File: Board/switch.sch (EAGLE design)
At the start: 15 parts, among them IC2 LM1117

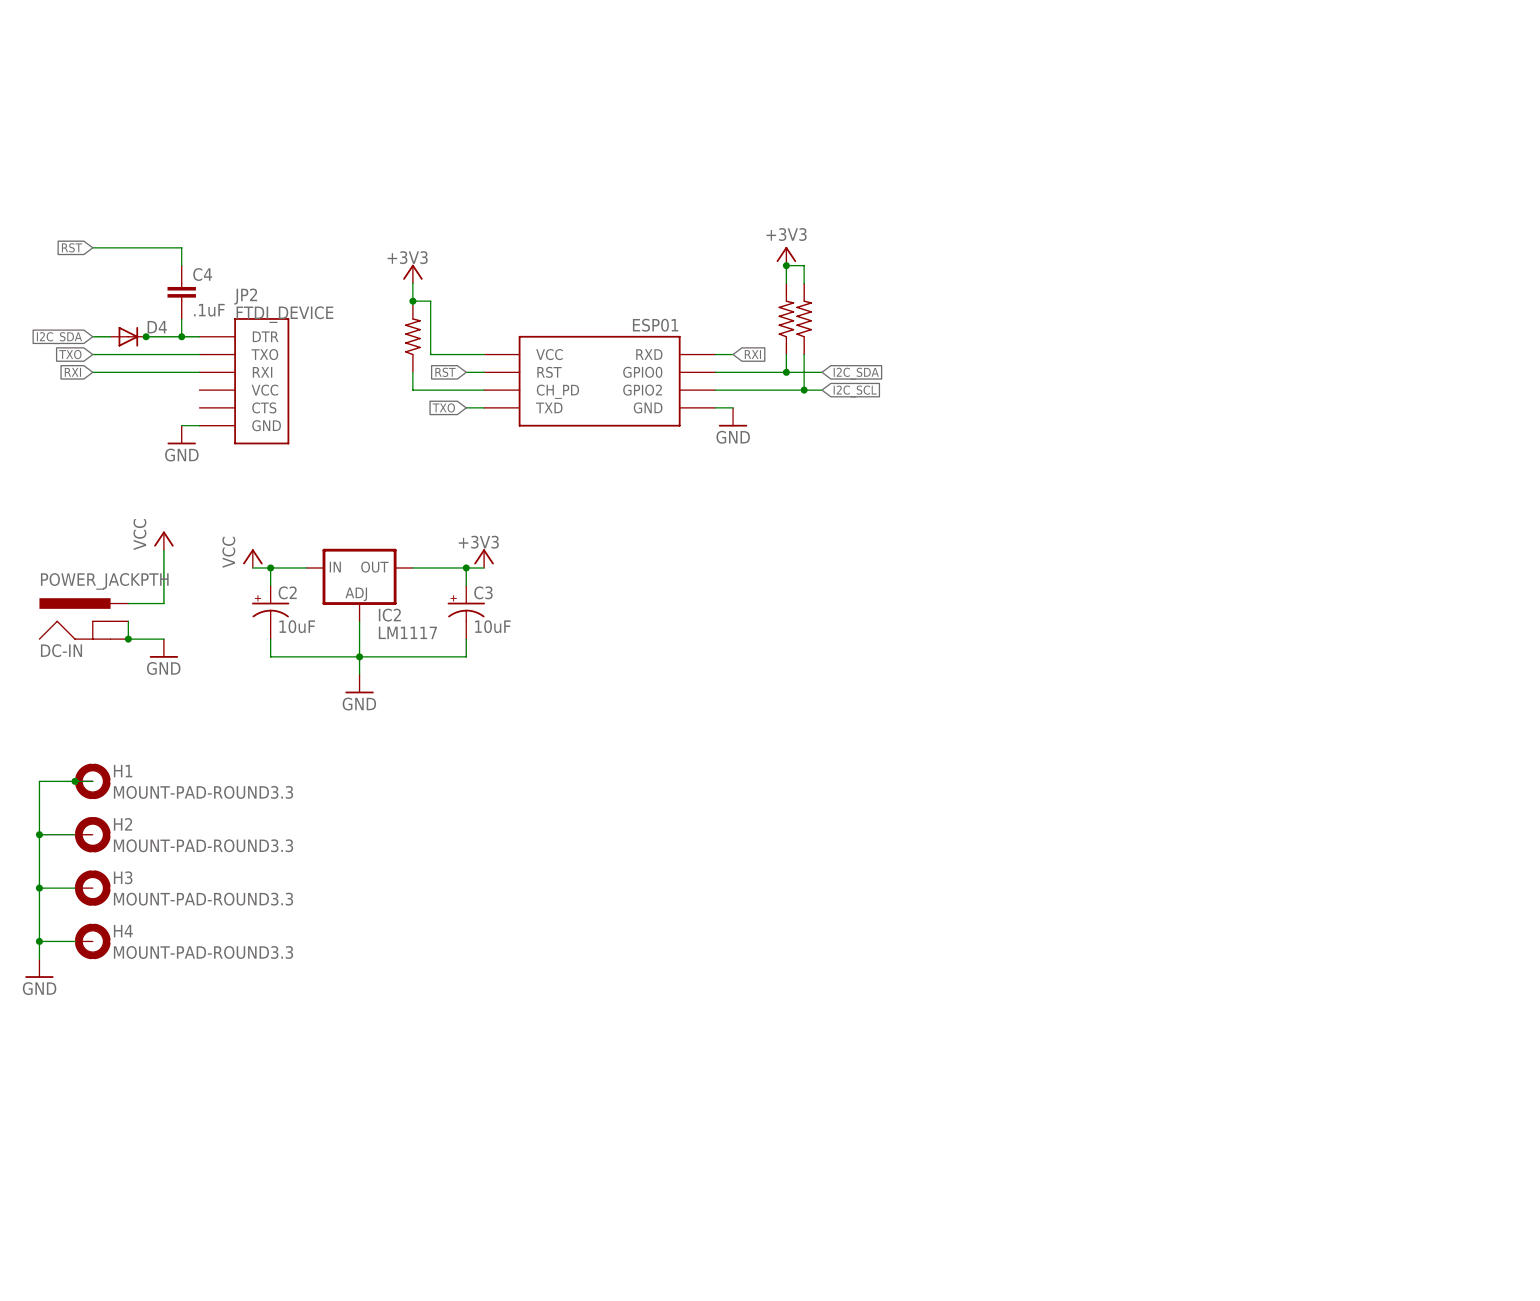
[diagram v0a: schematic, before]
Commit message: Add first pass board component layout
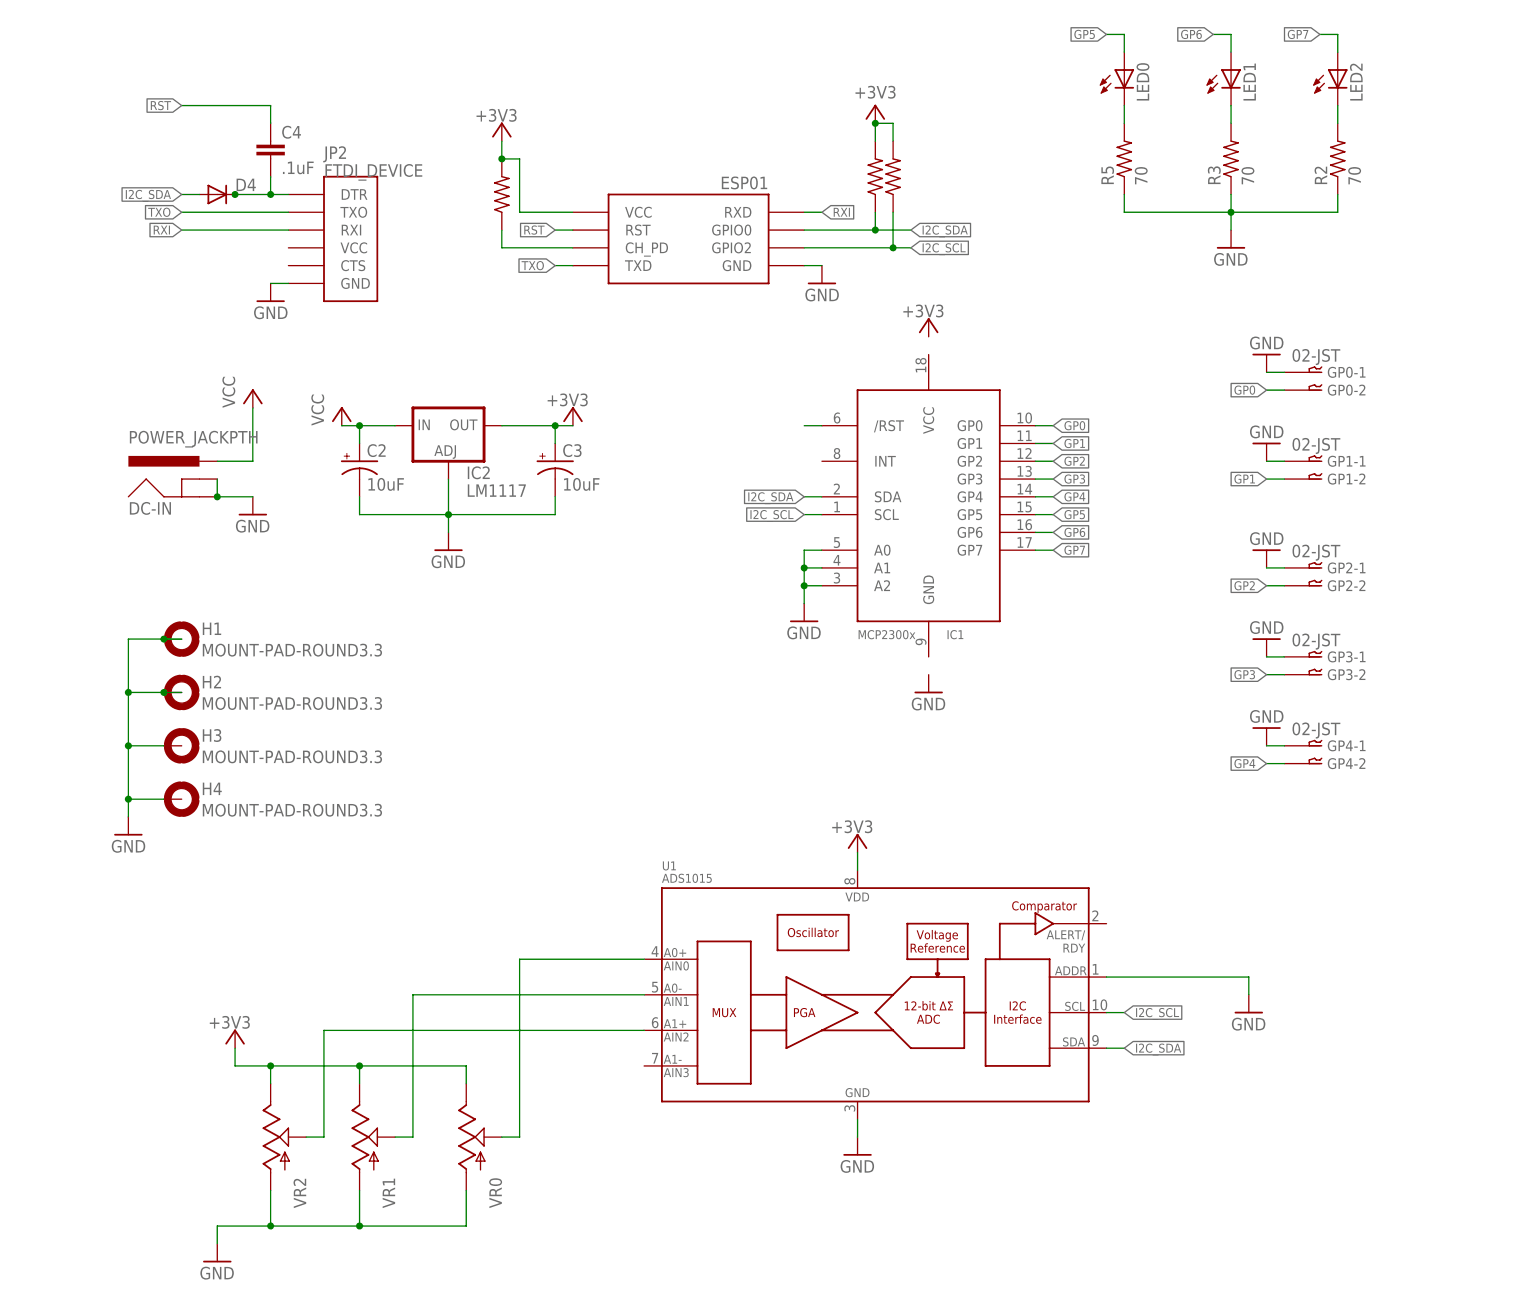
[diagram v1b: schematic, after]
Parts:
- added GP0, GP1, GP2, GP3, GP4: 02-JST, con-jst-xh:02-JST
- added IC1: MCP2300X/SO, adafruit:MCP2300X/SO
- added LED0, LED1, LED2: (no value), adafruit:LED3MM
- added R2, R3, R5: 70, resistor:R-US_R0603
- added U1: ADS1015, SparkFun-AnalogIC:ADS1015
- added VR0, VR1, VR2: (no value), SparkFun-Electromechanical:SLIDER30MM-KIT
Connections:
- new net DSD: GP2-1.1
- new net GP0: GP0-2.1, IC1.GP0
- new net GP1: GP1-2.1, IC1.GP1
- new net GP2: GP2-2.1, IC1.GP2
- new net GP3: GP3-2.1, IC1.GP3
- new net GP4: GP4-2.1, IC1.GP4
- new net GP5: IC1.GP5, LED0.A
- new net GP6: IC1.GP6, LED1.A
- new net GP7: IC1.GP7, LED2.A
- new net N$11: IC1./RST
- new net N$3: U1.AIN2, VR2.S
- new net N$4: U1.AIN1, VR1.S
- new net N$5: U1.AIN0, VR0.S
- new net N$6: LED0.C, R5.2
- new net N$7: LED1.C, R3.2
- new net N$8: LED2.C, R2.2
- net +3V3: now also U1.VDD, VR0.E, VR1.E, VR2.E
- net GND: now also GP0-1.1, GP1-1.1, GP3-1.1, GP4-1.1, IC1.A0, IC1.A1, IC1.A2, R2.1, R3.1, R5.1, U1.ADDR, U1.VSS, VR0.A, VR1.A, VR2.A
- net I2C_SCL: now also IC1.SCL, U1.SCL
- net I2C_SDA: now also IC1.SDA, U1.SDA
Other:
- moved on the sheet: C2, C3, C4, D4, DC-IN, H1, H2, H3, H4, IC2, JP2

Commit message: Use PTA3043 footprint for slider
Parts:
- VR0, VR1, VR2: device SparkFun-Electromechanical:SLIDER30MM-KIT -> SparkFun-Electromechanical:SLIDERPTA3043
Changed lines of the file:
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@@
 <grid distance="0.1" unitdist="inch" unit="inch" style="lines" multiple="1" display="no" altdistance="0.01" altunitdist="inch" altunit="inch"/>
 <layers>
-<layer number="1" name="Top" color="4" fill="1" visible="no" active="no"/>
-<layer number="2" name="Route2" color="1" fill="3" visible="no" active="no"/>
-<layer number="3" name="Route3" color="4" fill="3" visible="no" active="no"/>
-<layer number="14" name="Route14" color="1" fill="6" visible="no" active="no"/>
-<layer number="15" name="Route15" color="4" fill="6" visible="no" active="no"/>
-<layer number="16" name="Bottom" color="1" fill="1" visible="no" active="no"/>
-<layer number="17" name="Pads" color="2" fill="1" visible="no" active="no"/>
-<layer number="18" name="Vias" color="2" fill="1" visible="no" active="no"/>
-<layer number="19" name="Unrouted" color="6" fill="1" visible="no" active="no"/>
-<layer number="20" name="Dimension" color="15" fill="1" visible="no" active="no"/>
-<layer number="21" name="tPlace" color="7" fill="1" visible="no" active="no"/>
-<layer number="22" name="bPlace" color="7" fill="1" visible="no" active="no"/>
-<layer number="23" name="tOrigins" color="15" fill="1" visible="no" active="no"/>
-<layer number="24" name="bOrigins" color="15" fill="1" visible="no" active="no"/>
-<layer number="25" name="tNames" color="7" fill="1" visible="no" active="no"/>
-<layer number="26" name="bNames" color="7" fill="1" visible="no" active="no"/>
-<layer number="27" name="tValues" color="7" fill="1" visible="no" active="no"/>
-<layer number="28" name="bValues" color="7" fill="1" visible="no" active="no"/>
+<layer number="1" name="Top" color="4" fill="1" visible="yes" active="no"/>
+<layer number="2" name="Route2" color="1" fill="3" visible="yes" active="no"/>
+<layer number="3" name="Route3" color="4" fill="3" visible="yes" active="no"/>
+<layer number="14" name="Route14" color="1" fill="6" visible="yes" active="no"/>
+<layer number="15" name="Route15" color="4" fill="6" visible="yes" active="no"/>
+<layer number="16" name="Bottom" color="1" fill="1" visible="yes" active="no"/>
+<layer number="17" name="Pads" color="2" fill="1" visible="yes" active="no"/>
+<layer number="18" name="Vias" color="2" fill="1" visible="yes" active="no"/>
+<layer number="19" name="Unrouted" color="6" fill="1" visible="yes" active="no"/>
+<layer number="20" name="Dimension" color="15" fill="1" visible="yes" active="no"/>
+<layer number="21" name="tPlace" color="7" fill="1" visible="yes" active="no"/>
+<layer number="22" name="bPlace" color="7" fill="1" visible="yes" active="no"/>
+<layer number="23" name="tOrigins" color="15" fill="1" visible="yes" active="no"/>
+<layer number="24" name="bOrigins" color="15" fill="1" visible="yes" active="no"/>
+<layer number="25" name="tNames" color="7" fill="1" visible="yes" active="no"/>
+<layer number="26" name="bNames" color="7" fill="1" visible="yes" active="no"/>
+<layer number="27" name="tValues" color="7" fill="1" visible="yes" active="no"/>
+<layer number="28" name="bValues" color="7" fill="1" visible="yes" active="no"/>
 <layer number="29" name="tStop" color="7" fill="3" visible="no" active="no"/>
 <layer number="30" name="bStop" color="7" fill="6" visible="no" active="no"/>
@@
 <layer number="35" name="tGlue" color="7" fill="4" visible="no" active="no"/>
 <layer number="36" name="bGlue" color="7" fill="5" visible="no" active="no"/>
-<layer number="37" name="tTest" color="7" fill="1" visible="no" active="no"/>
-<layer number="38" name="bTest" color="7" fill="1" visible="no" active="no"/>
+<layer number="37" name="tTest" color="7" fill="1" visible="yes" active="no"/>
+<layer number="38" name="bTest" color="7" fill="1" visible="yes" active="no"/>
 <layer number="39" name="tKeepout" color="4" fill="11" visible="no" active="no"/>
 <layer number="40" name="bKeepout" color="1" fill="11" visible="no" active="no"/>
@@
 <layer number="44" name="Drills" color="7" fill="1" visible="no" active="no"/>
 <layer number="45" name="Holes" color="7" fill="1" visible="no" active="no"/>
-<layer number="46" name="Milling" color="3" fill="1" visible="no" active="no"/>
-<layer number="47" name="Measures" color="7" fill="1" visible="no" active="no"/>
-<layer number="48" name="Document" color="7" fill="1" visible="no" active="no"/>
-<layer number="49" name="Reference" color="7" fill="1" visible="no" active="no"/>
-<layer number="50" name="dxf" color="7" fill="1" visible="no" active="no"/>
-<layer number="51" name="tDocu" color="7" fill="1" visible="no" active="no"/>
-<layer number="52" name="bDocu" color="7" fill="1" visible="no" active="no"/>
-<layer number="53" name="tGND_GNDA" color="7" fill="1" visible="no" active="no"/>
-<layer number="54" name="bGND_GNDA" color="7" fill="1" visible="no" active="no"/>
-<layer number="56" name="wert" color="7" fill="1" visible="no" active="no"/>
-<layer number="57" name="tCAD" color="7" fill="1" visible="no" active="no"/>
-<layer number="59" name="tCarbon" color="7" fill="1" visible="no" active="no"/>
-<layer number="60" name="bCarbon" color="7" fill="1" visible="no" active="no"/>
+<layer number="46" name="Milling" color="3" fill="1" visible="yes" active="no"/>
+<layer number="47" name="Measures" color="7" fill="1" visible="yes" active="no"/>
+<layer number="48" name="Document" color="7" fill="1" visible="yes" active="no"/>
+<layer number="49" name="Reference" color="7" fill="1" visible="yes" active="no"/>
+<layer number="50" name="dxf" color="7" fill="1" visible="yes" active="no"/>
+<layer number="51" name="tDocu" color="7" fill="1" visible="yes" active="no"/>
+<layer number="52" name="bDocu" color="7" fill="1" visible="yes" active="no"/>
+<layer number="53" name="tGND_GNDA" color="7" fill="1" visible="yes" active="no"/>
+<layer number="54" name="bGND_GNDA" color="7" fill="1" visible="yes" active="no"/>
+<layer number="56" name="wert" color="7" fill="1" visible="yes" active="no"/>
+<layer number="57" name="tCAD" color="7" fill="1" visible="yes" active="no"/>
+<layer number="59" name="tCarbon" color="7" fill="1" visible="yes" active="no"/>
+<layer number="60" name="bCarbon" color="7" fill="1" visible="yes" active="no"/>
 <layer number="90" name="Modules" color="5" fill="1" visible="yes" active="yes"/>
 <layer number="91" name="Nets" color="2" fill="1" visible="yes" active="yes"/>
@@
 <part name="IC1" library="adafruit" deviceset="MCP2300X" device="/SO"/>
 <part name="U1" library="SparkFun-AnalogIC" deviceset="ADS1015" device="" value="ADS1015"/>
-<part name="VR2" library="SparkFun-Electromechanical" deviceset="SLIDER" device="30MM-KIT"/>
-<part name="VR1" library="SparkFun-Electromechanical" deviceset="SLIDER" device="30MM-KIT"/>
-<part name="VR0" library="SparkFun-Electromechanical" deviceset="SLIDER" device="30MM-KIT"/>
+<part name="VR2" library="SparkFun-Electromechanical" deviceset="SLIDER" device="PTA3043"/>
+<part name="VR1" library="SparkFun-Electromechanical" deviceset="SLIDER" device="PTA3043"/>
+<part name="VR0" library="SparkFun-Electromechanical" deviceset="SLIDER" device="PTA3043"/>
 <part name="+3V1" library="supply1" deviceset="+3V3" device=""/>
 <part name="GND1" library="supply1" deviceset="GND" device=""/>
